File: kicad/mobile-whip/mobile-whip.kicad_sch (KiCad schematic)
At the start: 54 parts, among them J1 SMA Edge Mount Male, J2 USB_C_Receptacle_USB2.0, Q1 SI2301CDS-T1-GE3, Q2 SI2301CDS-T1-GE3, SW1 MK-12C02-G025, U1 LTC6268IS6, U2 TP4054, U3 LP2985-3.3, U4 TLV431

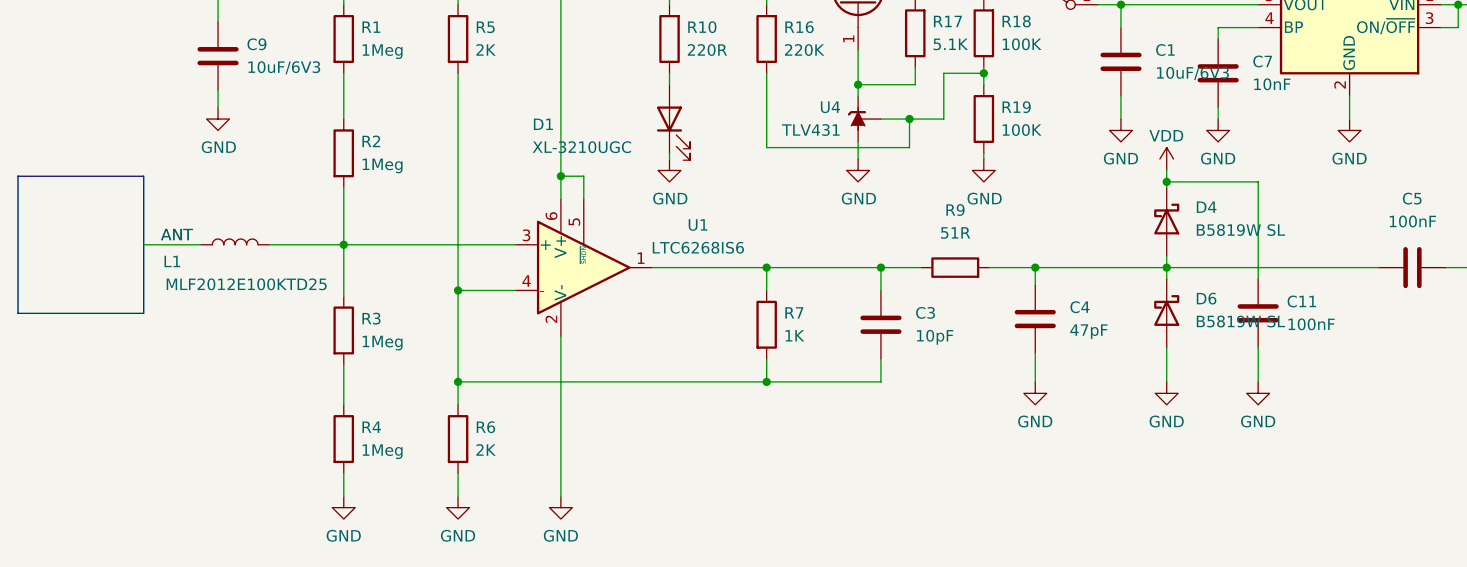
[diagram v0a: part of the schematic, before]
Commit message: Remove lowpass capacitors and short input inductor
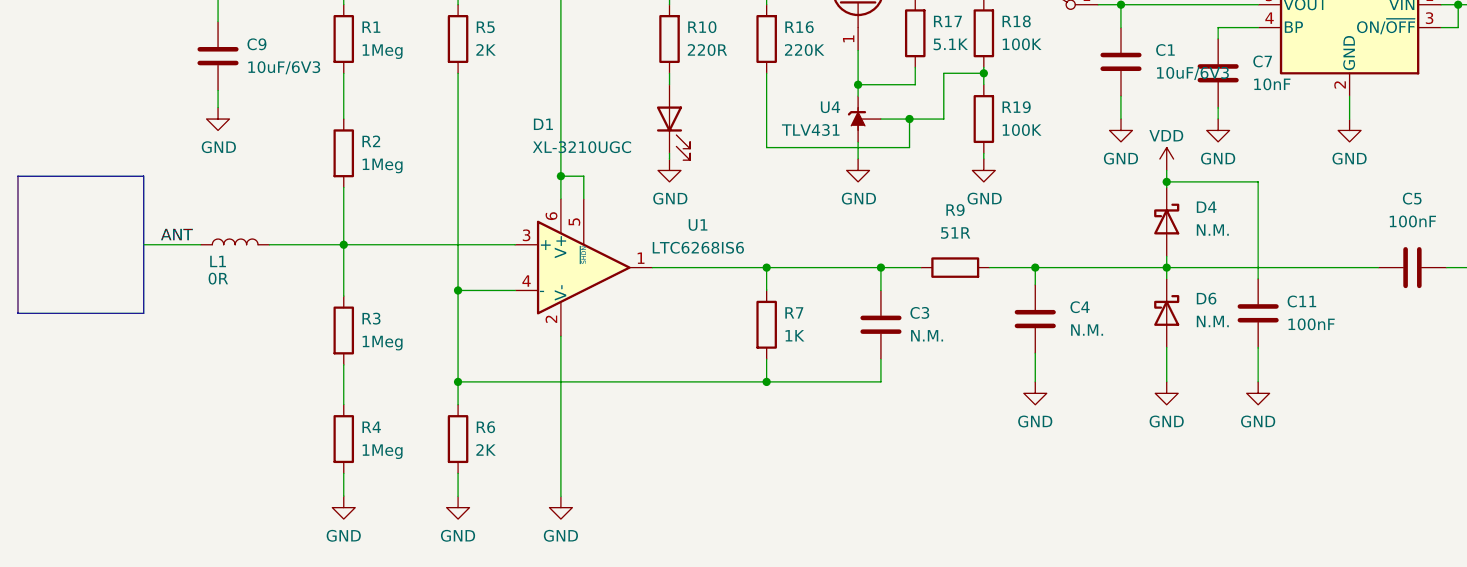
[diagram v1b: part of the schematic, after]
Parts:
- C3: value 10pF -> N.M.
- C4: value 47pF -> N.M.
- D4, D6: value B5819W SL -> N.M.
- L1: value MLF2012E100KTD25 -> 0R
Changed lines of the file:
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@@
       (effects (font (size 1.27 1.27)) (justify left))
     )
-    (property "Value" "47pF" (id 1) (at 130.81 118.7449 0)
+    (property "Value" "N.M." (id 1) (at 130.81 118.7449 0)
       (effects (font (size 1.27 1.27)) (justify left))
     )
@@
   (symbol (lib_id "Device:C") (at 109.855 118.11 0) (unit 1)
     (in_bom yes) (on_board yes) (fields_autoplaced)
-    (property "Reference" "C3" (id 0) (at 113.665 116.8399 0)
-      (effects (font (size 1.27 1.27)) (justify left))
-    )
-    (property "Value" "10pF" (id 1) (at 113.665 119.3799 0)
+    (property "Reference" "C3" (id 0) (at 113.03 116.8399 0)
+      (effects (font (size 1.27 1.27)) (justify left))
+    )
+    (property "Value" "N.M." (id 1) (at 113.03 119.3799 0)
       (effects (font (size 1.27 1.27)) (justify left))
     )
@@
       (effects (font (size 1.27 1.27)) (justify left))
     )
-    (property "Value" "B5819W SL" (id 1) (at 144.78 107.6324 90)
+    (property "Value" "N.M." (id 1) (at 144.78 107.6324 90)
       (effects (font (size 1.27 1.27)) (justify left))
     )
@@
   (symbol (lib_id "Device:L") (at 38.1 109.22 90) (unit 1)
     (in_bom yes) (on_board yes)
-    (property "Reference" "L1" (id 0) (at 31.115 111.125 90))
-    (property "Value" "MLF2012E100KTD25" (id 1) (at 39.37 113.665 90))
+    (property "Reference" "L1" (id 0) (at 36.195 111.125 90))
+    (property "Value" "0R" (id 1) (at 36.195 113.03 90))
     (property "Footprint" "Inductor_SMD:L_0805_2012Metric" (id 2) (at 38.1 109.22 0)
       (effects (font (size 1.27 1.27)) hide)
@@
       (effects (font (size 1.27 1.27)) (justify left))
     )
-    (property "Value" "B5819W SL" (id 1) (at 144.78 117.7924 90)
+    (property "Value" "N.M." (id 1) (at 144.78 117.7924 90)
       (effects (font (size 1.27 1.27)) (justify left))
     )
@@
     )
     (path "/6c408477-374e-46a4-b195-223418296e20"
-      (reference "C3") (unit 1) (value "10pF") (footprint "Capacitor_SMD:C_0805_2012Metric")
+      (reference "C3") (unit 1) (value "N.M.") (footprint "Capacitor_SMD:C_0805_2012Metric")
     )
     (path "/2675271d-548a-409a-9942-989ed6de53e0"
-      (reference "C4") (unit 1) (value "47pF") (footprint "Capacitor_SMD:C_0805_2012Metric")
+      (reference "C4") (unit 1) (value "N.M.") (footprint "Capacitor_SMD:C_0805_2012Metric")
     )
     (path "/3c5248a3-8f3f-476f-a470-b075e2a60306"
@@
     )
     (path "/850230a1-e985-4aec-bfc1-cca85f47f39d"
-      (reference "D4") (unit 1) (value "B5819W SL") (footprint "Diode_SMD:D_SOD-123")
+      (reference "D4") (unit 1) (value "N.M.") (footprint "Diode_SMD:D_SOD-123")
     )
     (path "/51d4da84-adfb-4a06-a39b-d200bf6f99a7"
@@
     )
     (path "/ff377cbc-6042-46e6-9644-84dbcdaf714a"
-      (reference "D6") (unit 1) (value "B5819W SL") (footprint "Diode_SMD:D_SOD-123")
+      (reference "D6") (unit 1) (value "N.M.") (footprint "Diode_SMD:D_SOD-123")
     )
     (path "/e12d1fdc-79fc-4b5e-8e8e-02d21fa57709"
@@
     )
     (path "/d99aad4d-8a7c-4eff-88b0-6cf9cb544a94"
-      (reference "L1") (unit 1) (value "MLF2012E100KTD25") (footprint "Inductor_SMD:L_0805_2012Metric")
+      (reference "L1") (unit 1) (value "0R") (footprint "Inductor_SMD:L_0805_2012Metric")
     )
     (path "/780daa5f-0411-4a9c-b0be-624b91dadf2d"
